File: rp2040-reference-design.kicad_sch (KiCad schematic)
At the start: 24 parts, among them J1 Conn_02x05_Odd_Even, SW1 SW_Push, SW2 SW_Push, U1 RP2040, U2 W25Q128JVS, Y1 12mhz ABM8-272-T

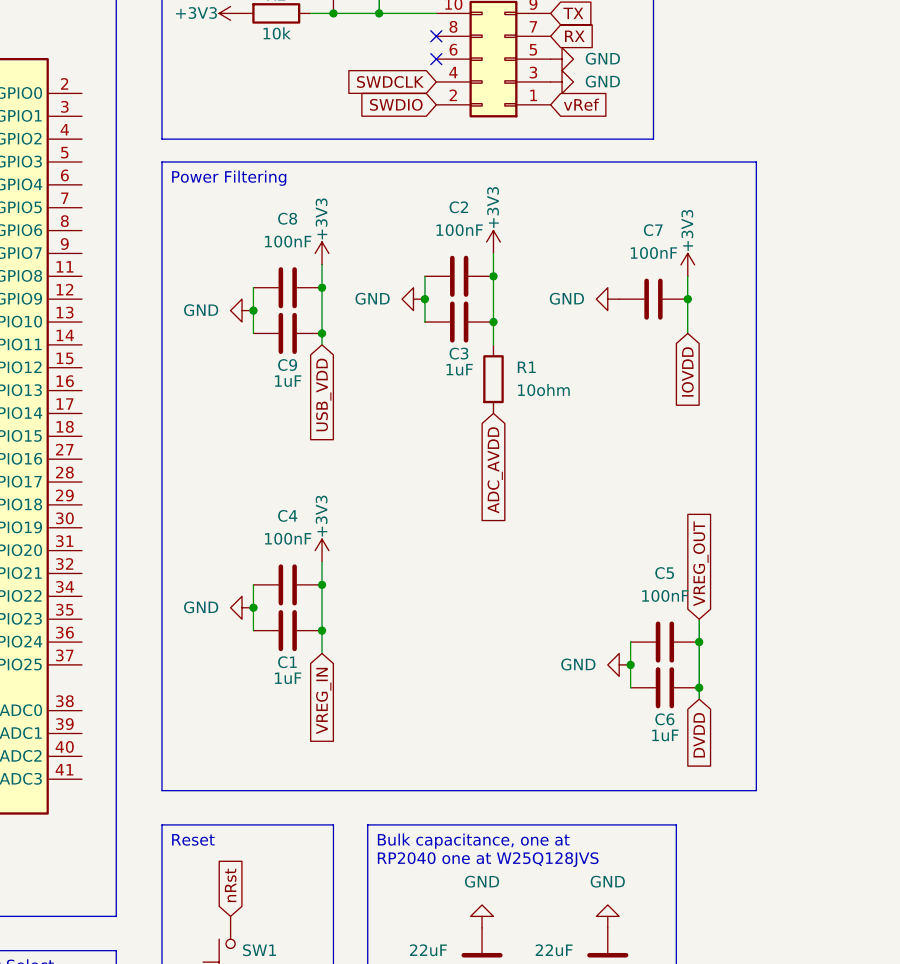
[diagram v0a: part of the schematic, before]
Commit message: fix: one cap per pin
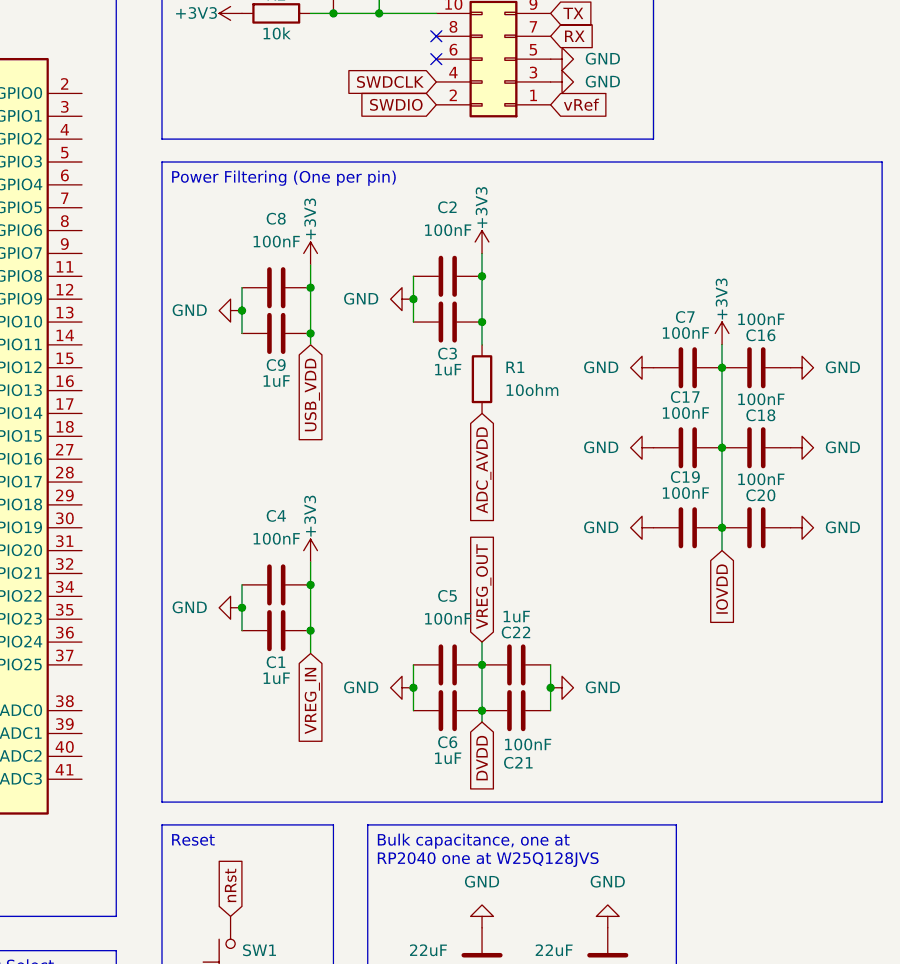
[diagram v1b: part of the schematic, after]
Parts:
- added C16, C17, C18, C19, C20, C21: 100nF, Capacitor_SMD:C_0402_1005Metric, symbol Device:C
- added C22: 1uF, Capacitor_SMD:C_0402_1005Metric, symbol Device:C
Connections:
- net +3V3: now also C16.2, C17.2, C18.2, C19.2, C20.2
- net DVDD: now also C21.2, C22.2
- net GND: now also C16.1, C17.1, C18.1, C19.1, C20.1, C21.1, C22.1
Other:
- moved on the sheet: C1, C2, C3, C4, C5, C6, C7, C8, C9, R1

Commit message: feat: led
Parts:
- added C23: 100nF, Capacitor_SMD:C_0402_1005Metric, symbol Device:C
- added D1: APA102-2020, LED_SMD:LED-APA102-2020, symbol LED:APA102-2020
- added R4, R5: 220ohm, Resistor_SMD:R_0402_1005Metric, symbol Device:R
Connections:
- net +3V3: now also C23.2, D1.1 (VDD)
- net GND: now also C23.1, D1.6 (GND)
- net CKI: now reaches U1.36 (GPIO24)
- net CKI: now also R5.1
- net SDI: now reaches U1.37 (GPIO25)
- net SDI: now also R4.1
- new net: D1.4 (SDI), R4.2
- new net: D1.5 (CKI), R5.2
- no-connect marks 2 -> 4
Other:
- moved on the sheet: C1, C10, C11, C12, C16, C17, C18, C19, C2, C20, C21, C22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

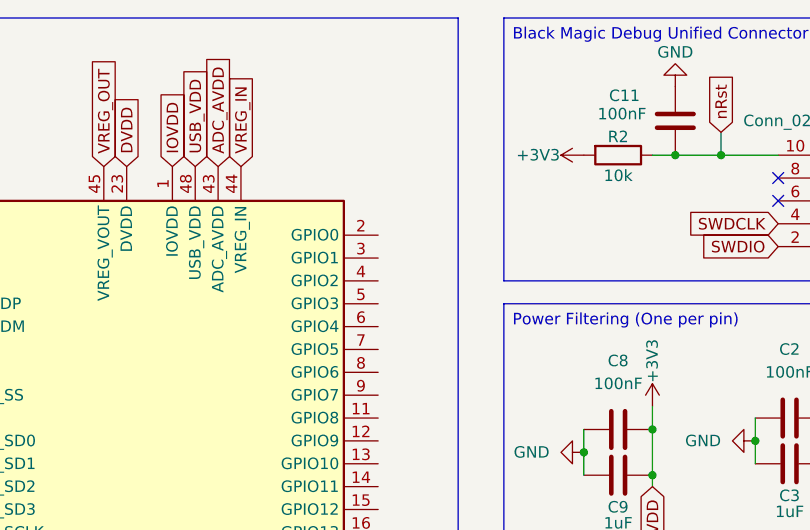
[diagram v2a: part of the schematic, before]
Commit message: fix: connectec uart
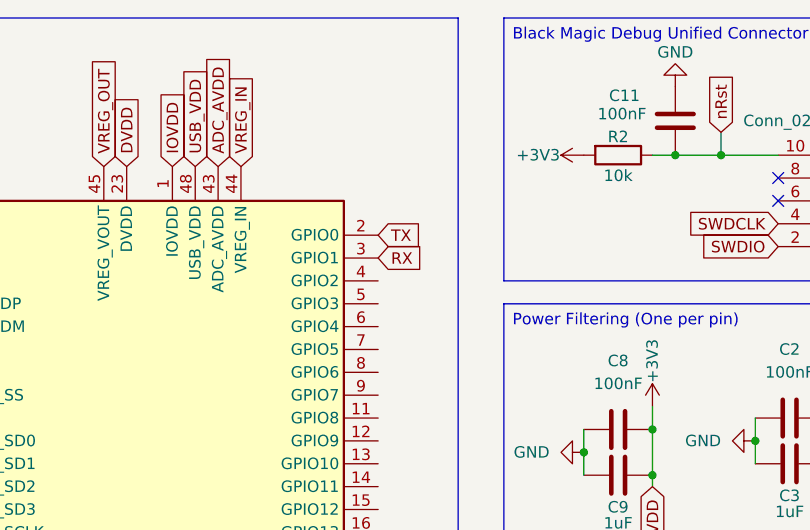
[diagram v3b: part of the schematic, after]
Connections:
- net RX: now also U1.3 (GPIO1)
- net TX: now also U1.2 (GPIO0)
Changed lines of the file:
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@@
+		)
+	)
+	(global_label "TX"
+		(shape input)
+		(at 93.98 43.18 0)
+		(fields_autoplaced yes)
+		(effects
+			(font
+				(size 1.27 1.27)
+			)
+			(justify left)
+		)
+		(property "Intersheetrefs" "${INTERSHEET_REFS}"
+			(at 99.1423 43.18 0)
+			(effects
+				(font
+					(size 1.27 1.27)
+				)
+				(justify left)
+				(hide yes)
+			)
 		)
 	)
@@
 				(hide yes)
 			)
+		)
+	)
+	(global_label "RX"
+		(shape input)
+		(at 93.98 45.72 0)
+		(fields_autoplaced yes)
+		(effects
+			(font
+				(size 1.27 1.27)
+			)
+			(justify left)
+		)
+		(property "Intersheetrefs" "${INTERSHEET_REFS}"
+			(at 99.4447 45.72 0)
+			(effects
+				(font
+					(size 1.27 1.27)
+				)
+				(justify left)
+				(hide yes)
+			)

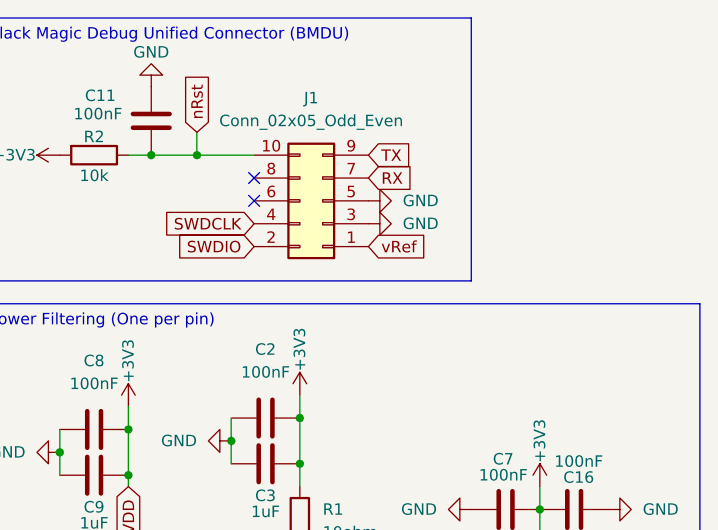
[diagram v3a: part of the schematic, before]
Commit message: fix: connected vref
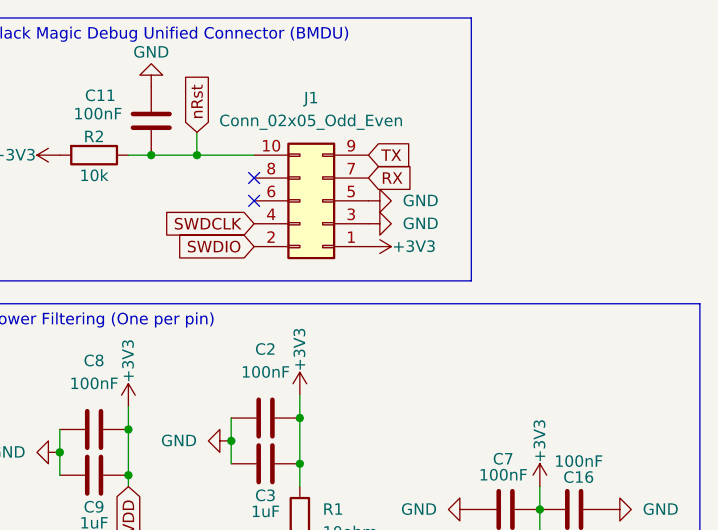
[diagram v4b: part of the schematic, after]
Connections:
- net vRef is gone; now on net +3V3: J1.1 (Pin_1)
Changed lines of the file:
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@@
 		)
 	)
-	(global_label "vRef"
-		(shape input)
-		(at 151.13 44.45 0)
-		(fields_autoplaced yes)
-		(effects
-			(font
-				(size 1.27 1.27)
-			)
-			(justify left)
-		)
-		(property "Intersheetrefs" "${INTERSHEET_REFS}"
-			(at 158.1671 44.45 0)
-			(effects
-				(font
-					(size 1.27 1.27)
-				)
-				(justify left)
-				(hide yes)
-			)
-		)
-	)
 	(global_label "SWDCLK"
 		(shape input)
@@
 					(unit 1)
 				)
+			)
+		)
+	)
+	(symbol
+		(lib_id "power:+3V3")
+		(at 151.13 44.45 270)
+		(unit 1)
+		(exclude_from_sim no)
+		(in_bom yes)
+		(on_board yes)
+		(dnp no)
+		(property "Reference" "#PWR039"
+			(at 147.32 44.45 0)
+			(effects
+				(font
+					(size 1.27 1.27)
+				)
+				(hide yes)
+			)
+		)
+		(property "Value" "+3V3"
+			(at 156.21 44.45 90)
+			(effects
+				(font
+					(size 1.27 1.27)
+				)
+			)
+		)
+		(property "Footprint" ""
+			(at 151.13 44.45 0)
+			(effects
+				(font
+					(size 1.27 1.27)
+				)
+				(hide yes)
+			)
+		)
+		(property "Datasheet" ""
+			(at 151.13 44.45 0)
+			(effects
+				(font
+					(size 1.27 1.27)
+				)
+				(hide yes)
+			)
+		)
+		(property "Description" "Power symbol creates a global label with name \"+3V3\""
+			(at 151.13 44.45 0)
+			(effects
+				(font
+					(size 1.27 1.27)
+				)
+				(hide yes)
+			)
+		)
+		(pin "1"
+		)
+		(instances
+			(project "rp2040-reference-design"
+				(path "/d9eb9251-8b4f-4594-87db-d1b592086b55"
+					(reference "#PWR039")
+					(unit 1)
+				)

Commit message: feat: reference layout
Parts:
- removed C1: 1uF, Capacitor_SMD:C_0402_1005Metric, symbol Device:C
- removed C20, C4: 100nF, Capacitor_SMD:C_0402_1005Metric, symbol Device:C
- added J2, J3: Conn_01x10_Pin, Connector_PinSocket_2.54mm:PinSocket_1x10_P2.54mm_Vertical, symbol Connector:Conn_01x10_Pin
- added R6: 220ohm, Resistor_SMD:R_0402_1005Metric, symbol Device:R
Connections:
- net +3V3: now also J3.10 (Pin_10)
- net GND: now also J3.9 (Pin_9)
- net QSPI_SS: now also R6.2; no longer SW2.2
- net GPIO8: now reaches U1.11 (GPIO8)
- net GPIO8: now also J2.7 (Pin_7)
- net GPIO9: now reaches U1.12 (GPIO9)
- net GPIO9: now also J2.8 (Pin_8)
- net GPIO10: now reaches U1.13 (GPIO10)
- net GPIO10: now also J2.9 (Pin_9)
- net GPIO11: now reaches U1.14 (GPIO11)
- net GPIO11: now also J2.10 (Pin_10)
- net GPIO12: now reaches U1.15 (GPIO12)
- net GPIO12: now also J3.8 (Pin_8)
- net GPIO13: now reaches U1.16 (GPIO13)
- net GPIO13: now also J3.7 (Pin_7)
- net GPIO14: now reaches U1.17 (GPIO14)
- net GPIO14: now also J3.6 (Pin_6)
- net GPIO15: now reaches U1.18 (GPIO15)
- net GPIO15: now also J3.5 (Pin_5)
- net GPIO16: now reaches U1.27 (GPIO16)
- net GPIO16: now also J3.4 (Pin_4)
- net GPIO17: now reaches U1.28 (GPIO17)
- net GPIO17: now also J3.3 (Pin_3)
- net GPIO18: now reaches U1.29 (GPIO18)
- net GPIO18: now also J3.2 (Pin_2)
- net GPIO19: now reaches U1.30 (GPIO19)
- net GPIO19: now also J3.1 (Pin_1)
- net GPIO20: now reaches U1.31 (GPIO20)
- net GPIO21: now reaches U1.32 (GPIO21)
- net GPIO22: now reaches U1.34 (GPIO22)
- net GPIO23: now reaches U1.35 (GPIO23)
- net GPIO2: now reaches U1.4 (GPIO2)
- net GPIO2: now also J2.1 (Pin_1)
- net GPIO3: now reaches U1.5 (GPIO3)
- net GPIO3: now also J2.2 (Pin_2)
- net GPIO4: now reaches U1.6 (GPIO4)
- net GPIO4: now also J2.3 (Pin_3)
- net GPIO5: now reaches U1.7 (GPIO5)
- net GPIO5: now also J2.4 (Pin_4)
- net GPIO6: now reaches U1.8 (GPIO6)
- net GPIO6: now also J2.5 (Pin_5)
- net GPIO7: now reaches U1.9 (GPIO7)
- net GPIO7: now also J2.6 (Pin_6)
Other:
- moved on the sheet: C10, C11, C12, C16, C17, C18, C19, C2, C21, C22, C23, C3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

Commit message: fix: drc
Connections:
- net at R6.1: now also SW2.2
- no-connect marks 4 -> 8
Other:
- moved on the sheet: SW2
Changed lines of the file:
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@@
 	)
 	(no_connect
+		(at 93.98 111.76)
+	)
+	(no_connect
 		(at 146.05 39.37)
 	)
 	(no_connect
+		(at 93.98 116.84)
+	)
+	(no_connect
+		(at 93.98 119.38)
+	)
+	(no_connect
 		(at 147.32 175.26)
 	)
+	(no_connect
+		(at 93.98 114.3)
+	)
 	(wire
 		(pts
@@
 	(symbol
 		(lib_id "power:GND")
-		(at 86.36 168.91 0)
+		(at 86.36 170.18 0)
 		(unit 1)
 		(exclude_from_sim no)
@@
 		(fields_autoplaced yes)
 		(property "Reference" "#PWR016"
-			(at 86.36 175.26 0)
+			(at 86.36 176.53 0)
 			(effects
 				(font
@@
 		)
 		(property "Value" "GND"
-			(at 86.36 173.99 0)
+			(at 86.36 175.26 0)
 			(effects
 				(font
@@
 		)
 		(property "Footprint" ""
-			(at 86.36 168.91 0)
+			(at 86.36 170.18 0)
 			(effects
 				(font
@@
 		)
 		(property "Datasheet" ""
-			(at 86.36 168.91 0)
+			(at 86.36 170.18 0)
 			(effects
 				(font
@@
 		)
 		(property "Description" "Power symbol creates a global label with name \"GND\" , ground"
-			(at 86.36 168.91 0)
+			(at 86.36 170.18 0)
 			(effects
 				(font
@@
 	(symbol
 		(lib_id "Switch:SW_Push")
-		(at 86.36 163.83 90)
+		(at 86.36 165.1 90)
 		(unit 1)
 		(exclude_from_sim no)
@@
 		(fields_autoplaced yes)
 		(property "Reference" "SW2"
-			(at 87.63 162.5599 90)
+			(at 87.63 163.8299 90)
 			(effects
 				(font
@@
 		)
 		(property "Value" "SW_Push"
-			(at 87.63 165.0999 90)
+			(at 87.63 166.3699 90)
 			(effects
 				(font
@@
 		)
 		(property "Footprint" "Button_Switch_SMD:SW_SPST_EVQP7A"
-			(at 81.28 163.83 0)
+			(at 81.28 165.1 0)
 			(effects
 				(font
@@
 		)
 		(property "Datasheet" "~"
-			(at 81.28 163.83 0)
+			(at 81.28 165.1 0)
 			(effects
 				(font
@@
 		)
 		(property "Description" "Push button switch, generic, two pins"
-			(at 86.36 163.83 0)
+			(at 86.36 165.1 0)
 			(effects
 				(font

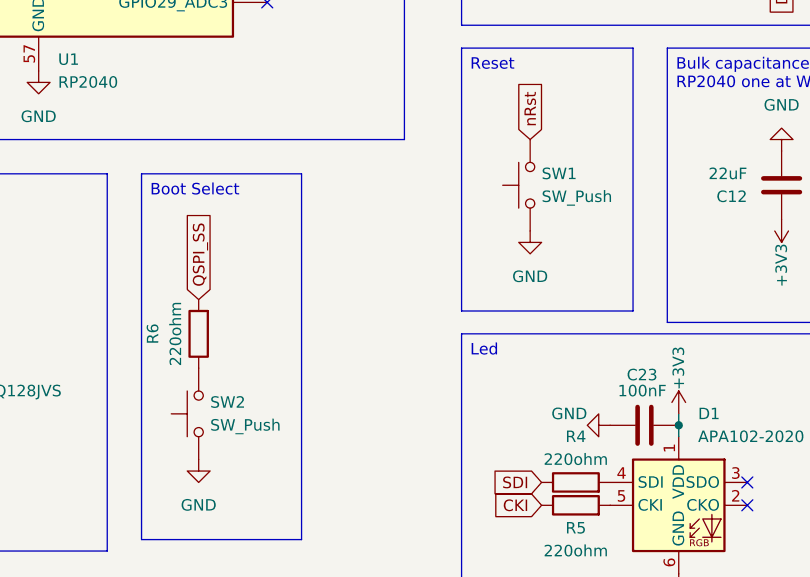
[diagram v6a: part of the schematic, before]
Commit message: fix: button text
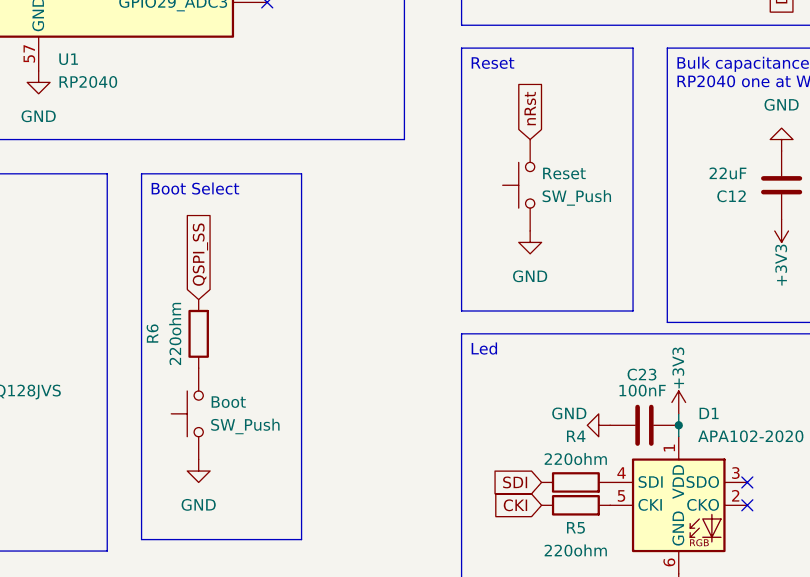
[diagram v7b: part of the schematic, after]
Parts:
- renumbered SW2 to Boot, SW1 to Reset
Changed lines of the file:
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@@
 		(dnp no)
 		(fields_autoplaced yes)
-		(property "Reference" "SW1"
+		(property "Reference" "Reset"
 			(at 124.46 138.4299 90)
 			(effects
@@
 			(project ""
 				(path "/d9eb9251-8b4f-4594-87db-d1b592086b55"
-					(reference "SW1")
+					(reference "Reset")
 					(unit 1)
 				)
@@
 		(dnp no)
 		(fields_autoplaced yes)
-		(property "Reference" "SW2"
+		(property "Reference" "Boot"
 			(at 87.63 163.8299 90)
 			(effects
@@
 			(project "rp2040-reference-design"
 				(path "/d9eb9251-8b4f-4594-87db-d1b592086b55"
-					(reference "SW2")
+					(reference "Boot")
 					(unit 1)
 				)

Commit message: feat: annotated stuff
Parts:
- renumbered J1 to BMDU
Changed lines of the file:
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@@
 		(dnp no)
 		(fields_autoplaced yes)
-		(property "Reference" "J1"
+		(property "Reference" "BMDU"
 			(at 152.4 27.94 0)
 			(effects
@@
 			(project ""
 				(path "/d9eb9251-8b4f-4594-87db-d1b592086b55"
-					(reference "J1")
+					(reference "BMDU")
 					(unit 1)
 				)
